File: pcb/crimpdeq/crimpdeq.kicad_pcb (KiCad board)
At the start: 4 copper layers, 30 x 30 mm, 51 parts, among them J2 USB4105-GF-A, J3 Loadcell_Pads, J4 Power_Sense_Pads, Q1 SS8550, Q2 DMG3415U, U1 ESP32-C3-MINI-1, U2 MCP73831T-2ACI/OT, U3 HX711, U5 MAX17048G+T10, U6 SY8088

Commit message: feat: split cable pads into independent battery and sense points
Replace the shared J4 multi-pad header with separate THT pads so B+/B-,
SW+/SW-, and A+/A- can be wired independently, and place the battery
column clear of USB/power copper.

Co-authored-by: Cursor <cursoragent@cursor.com>
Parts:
- removed J4: Power_Sense_Pads, External_Cable_Pads_Right
- added J10: A-_Cable_Pad, TestPoint:TestPoint_THTPad_D1.5mm_Drill0.7mm, F.Cu at (131.6, 81.1)
- added J5: B-_Cable_Pad, TestPoint:TestPoint_THTPad_D1.5mm_Drill0.7mm, F.Cu at (156.2, 73.5)
- added J6: SW+_Cable_Pad, TestPoint:TestPoint_THTPad_D1.5mm_Drill0.7mm, F.Cu at (156.2, 78.5)
- added J7: B+_Cable_Pad, TestPoint:TestPoint_THTPad_D1.5mm_Drill0.7mm, F.Cu at (156.2, 76.0)
- added J8: SW-_Cable_Pad, TestPoint:TestPoint_THTPad_D1.5mm_Drill0.7mm, F.Cu at (156.2, 81.1)
- added J9: A+_Cable_Pad, TestPoint:TestPoint_THTPad_D1.5mm_Drill0.7mm, F.Cu at (134.4, 81.1)
- R20, R21, R22: footprint R_0402_1005Metric -> Resistor_SMD:R_0402_1005Metric
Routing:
- net +BATT: track 43.7 -> 47.4 mm, vias 2 -> 3
- net SW_BATT: track 11.7 -> 13.8 mm
- net GND: track 215.7 -> 217.7 mm
- net VBUS: vias 2 -> 3
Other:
- board text added: "A+"
- board text added: "A-"
- board text added: "B+"
- board text added: "B-"
- board text added: "SW+"
- board text added: "SW-"

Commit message: fix: clean up cable-pad silk, Q2 symbol, and verification golden
Align the board with the post-split review: correct silk and shell vias,
use a pin-compatible PMOS symbol for DMG3415U, and update BOM/CPL/verify
for independent J5–J10 pads.

Co-authored-by: Cursor <cursoragent@cursor.com>
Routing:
- net Net-(J2-SHELL_GND-PadS1): track 33.6 -> 35.0 mm
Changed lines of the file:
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@@
 			(at 0 -1.648 0)
 			(layer "F.SilkS")
+			(hide yes)
 			(effects
 				(font
@@
 			(at 0 1.75 0)
 			(layer "F.Fab")
+			(hide yes)
 			(effects
 				(font
@@
 		(sheetname "/")
 		(sheetfile "crimpdeq.kicad_sch")
-		(units
-			(unit
-				(name "A")
-				(pins "1" "2")
-			)
-		)
 		(attr smd)
 		(duplicate_pad_numbers_are_jumpers no)
@@
 			(at 0 -1.648 0)
 			(layer "F.SilkS")
+			(hide yes)
 			(effects
 				(font
@@
 			(at 0 -1.648 0)
 			(layer "F.SilkS")
+			(hide yes)
 			(effects
 				(font
@@
 		(sheetname "/")
 		(sheetfile "crimpdeq.kicad_sch")
-		(units
-			(unit
-				(name "A")
-				(pins "1" "2")
-			)
-		)
 		(attr smd)
 		(duplicate_pad_numbers_are_jumpers no)
@@
 			(at 0 -1.648 0)
 			(layer "F.SilkS")
+			(hide yes)
 			(effects
 				(font
@@
 			(at 0 1.75 0)
 			(layer "F.Fab")
+			(hide yes)
 			(effects
 				(font
@@
 			(at 0 -1.648 0)
 			(layer "F.SilkS")
+			(hide yes)
 			(effects
 				(font
@@
 			(at 0 -1.648 0)
 			(layer "F.SilkS")
+			(hide yes)
 			(effects
 				(font
@@
 		(layer "Edge.Cuts")
 	)
-	(gr_text "SW+"
-		(at 154.5 66.7 0)
-		(layer "F.SilkS")
-		(effects
-			(font
-				(size 0.7 0.7)
-				(thickness 0.105)
-			)
-		)
-	)
-	(gr_text "SW-"
-		(at 154.5 69.3 0)
-		(layer "F.SilkS")
-		(effects
-			(font
-				(size 0.7 0.7)
-				(thickness 0.105)
-			)
-		)
-	)
-	(gr_text "B-"
-		(at 154.7 61.5 0)
-		(layer "F.SilkS")
-		(effects
-			(font
-				(size 0.7 0.7)
-				(thickness 0.105)
-			)
-		)
-	)
-	(gr_text "B+"
-		(at 154.7 64.099999 0)
-		(layer "F.SilkS")
-		(effects
-			(font
-				(size 0.7 0.7)
-				(thickness 0.105)
-			)
-		)
-	)
 	(gr_text "A-"
-		(at 131.6 79.7 0)
+		(at 131.6 79.5 0)
 		(layer "F.SilkS")
 		(effects
@@
 	)
 	(gr_text "A+"
-		(at 134.4 79.7 0)
+		(at 134.4 79.5 0)
 		(layer "F.SilkS")
 		(effects
@@
 		)
 	)
-	(gr_text "SW+"
-		(at 151.8 79.2 0)
+	(gr_text "B-"
+		(at 153.5 73.5 0)
 		(layer "F.SilkS")
 		(effects
@@
 		)
 	)
-	(gr_text "B+"
-		(at 152.3 76.2 0)
+	(gr_text "SW+"
+		(at 153.8 78.55 0)
 		(layer "F.SilkS")
 		(effects
@@
 	)
 	(gr_text "SW-"
-		(at 155.2 79.2 0)
+		(at 153.8 81.1 0)
 		(layer "F.SilkS")
 		(effects
@@
 		)
 	)
-	(gr_text "B-"
-		(at 155.5 75.7 0)
+	(gr_text "B+"
+		(at 154 76 0)
 		(layer "F.SilkS")
 		(effects
@@
 	)
 	(segment
+		(start 152 76)
+		(end 151.32 76)
+		(width 0.25)
+		(layer "B.Cu")
+		(net "Net-(J2-SHELL_GND-PadS1)")
+	)
+	(segment
 		(start 146.49 70.5)
 		(end 141 70.5)
@@
 		(layer "B.Cu")
 		(net "Net-(J2-SHELL_GND-PadS1)")
+	)
+	(segment
+		(start 142 76)
+		(end 142.68 76)
+		(width 0.25)
+		(layer "B.Cu")
+		(net "Net-(J2-SHELL_GND-PadS1)")

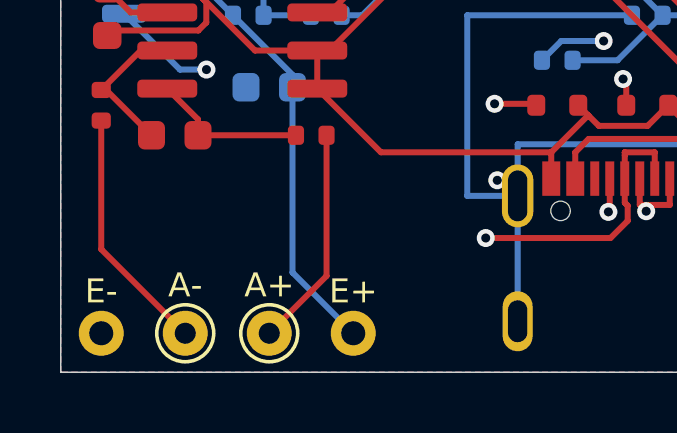
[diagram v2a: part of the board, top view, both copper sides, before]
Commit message: feat: replace J3/U4 with independent E+ and E- cable pads
Make excitation pads match the other single-pad connectors, drop the
board-only J3 footprint and U4 harness symbol, and refresh schematic
layout plus verification/assembly artifacts.

Co-authored-by: Cursor <cursoragent@cursor.com>
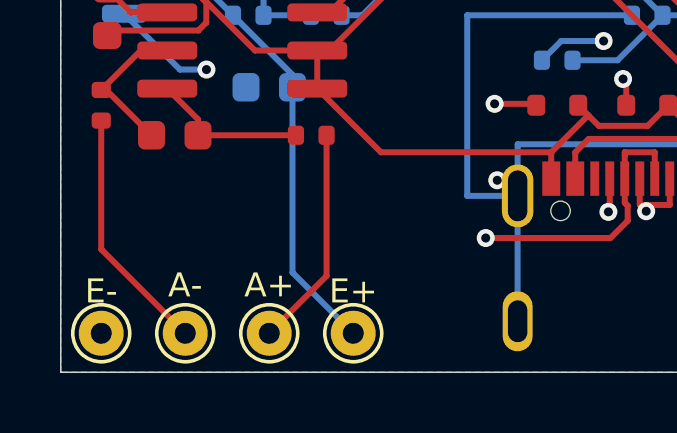
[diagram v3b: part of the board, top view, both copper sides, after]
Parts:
- removed J3: Loadcell_Pads, External_Cable_Pads_Left
- added J11: E+_Cable_Pad, TestPoint:TestPoint_THTPad_D1.5mm_Drill0.7mm, F.Cu at (137.2, 81.1)
- added J12: E-_Cable_Pad, TestPoint:TestPoint_THTPad_D1.5mm_Drill0.7mm, F.Cu at (128.8, 81.1)
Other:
- board text added: "E+"
- board text added: "E-"
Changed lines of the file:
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@@
 		)
 	)
-	(footprint "External_Cable_Pads_Left"
-		(layer "F.Cu")
-		(at 151.2 55.75)
-		(property "Reference" "J3"
-			(at 0 -4 0)
-			(layer "F.SilkS")
-			(hide yes)
-			(effects
-				(font
-					(size 1 1)
-					(thickness 0.15)
-				)
-			)
-		)
-		(property "Value" "Loadcell_Pads"
-			(at 0 4 0)
-			(layer "F.Fab")
-			(hide yes)
-			(effects
-				(font
-					(size 1 1)
-					(thickness 0.15)
-				)
-			)
-		)
-		(property "Datasheet" ""
-			(at 0 0 0)
-			(layer "F.Fab")
-			(hide yes)
-			(effects
-				(font
-					(size 1 1)
-					(thickness 0.15)
-				)
-			)
-		)
-		(property "Description" ""
-			(at 0 0 0)
-			(layer "F.Fab")
-			(hide yes)
-			(effects
-				(font
-					(size 1 1)
-					(thickness 0.15)
-				)
-			)
-		)
-		(attr through_hole board_only)
-		(duplicate_pad_numbers_are_jumpers no)
-		(fp_text user "E-"
-			(at -22.4 23.95 0)
-			(layer "F.SilkS")
-			(effects
-				(font
-					(size 0.8 0.8)
-					(thickness 0.15)
-				)
-			)
-		)
-		(fp_text user "E+"
-			(at -14 23.95 0)
-			(layer "F.SilkS")
-			(effects
-				(font
-					(size 0.8 0.8)
-					(thickness 0.15)
-				)
-			)
-		)
-		(pad "1" thru_hole circle
-			(at -14 25.35)
-			(size 1.5 1.5)
-			(drill 0.8)
-			(layers "*.Cu" "*.Mask")
-			(remove_unused_layers no)
-			(net "E+")
-			(pinfunction "E+")
-			(pintype "passive")
-		)
-		(pad "2" thru_hole circle
-			(at -22.4 25.35)
-			(size 1.5 1.5)
-			(drill 0.8)
-			(layers "*.Cu" "*.Mask")
-			(remove_unused_layers no)
-			(net "GND")
-			(pinfunction "E-")
-			(pintype "passive")
-		)
-		(embedded_fonts no)
-	)
 	(footprint "Resistor_SMD:R_0402_1005Metric"
 		(layer "F.Cu")
@@
 	(footprint "TestPoint:TestPoint_THTPad_D1.5mm_Drill0.7mm"
 		(layer "F.Cu")
+		(at 137.2 81.1)
+		(descr "THT pad as test Point, diameter 1.5mm, hole diameter 0.7mm")
+		(tags "test point THT pad")
+		(property "Reference" "J11"
+			(at 0 -1.648 0)
+			(layer "F.SilkS")
+			(hide yes)
+			(effects
+				(font
+					(size 1 1)
+					(thickness 0.15)
+				)
+			)
+		)
+		(property "Value" "E+_Cable_Pad"
+			(at 0 1.75 0)
+			(layer "F.Fab")
+			(hide yes)
+			(effects
+				(font
+					(size 1 1)
+					(thickness 0.15)
+				)
+			)
+		)
+		(property "Datasheet" ""
+			(at 0 0 0)
+			(unlocked yes)
+			(layer "F.Fab")
+			(hide yes)
+			(effects
+				(font
+					(size 1.27 1.27)
+					(thickness 0.15)
+				)
+			)
+		)
+		(property "Description" ""
+			(at 0 0 0)
+			(unlocked yes)
+			(layer "F.Fab")
+			(hide yes)
+			(effects
+				(font
+					(size 1.27 1.27)
+					(thickness 0.15)
+				)
+			)
+		)
+		(duplicate_pad_numbers_are_jumpers no)
+		(fp_circle
+			(center 0 0)
+			(end 0 0.95)
+			(stroke
+				(width 0.12)
+				(type solid)
+			)
+			(fill no)
+			(layer "F.SilkS")
+		)
+		(fp_circle
+			(center 0 0)
+			(end 1.25 0)
+			(stroke
+				(width 0.05)
+				(type solid)
+			)
+			(fill no)
+			(layer "F.CrtYd")
+		)
+		(fp_text user "${REFERENCE}"
+			(at 0 -1.65 0)
+			(layer "F.Fab")
+			(effects
+				(font
+					(size 1 1)
+					(thickness 0.15)
+				)
+			)
+		)
+		(pad "1" thru_hole circle
+			(at 0 0)
+			(size 1.5 1.5)
+			(drill 0.7)
+			(layers "*.Cu" "*.Mask")
+			(remove_unused_layers no)
+			(net "E+")
+		)
+		(embedded_fonts no)
+	)
+	(footprint "TestPoint:TestPoint_THTPad_D1.5mm_Drill0.7mm"
+		(layer "F.Cu")
 		(at 131.6 81.1)
 		(descr "THT pad as test Point, diameter 1.5mm, hole diameter 0.7mm")
@@
 		)
 	)
+	(footprint "TestPoint:TestPoint_THTPad_D1.5mm_Drill0.7mm"
+		(layer "F.Cu")
+		(at 128.8 81.1)
+		(descr "THT pad as test Point, diameter 1.5mm, hole diameter 0.7mm")
+		(tags "test point THT pad")
+		(property "Reference" "J12"
+			(at 0 -1.648 0)
+			(layer "F.SilkS")
+			(hide yes)
+			(effects
+				(font
+					(size 1 1)
+					(thickness 0.15)
+				)
+			)
+		)
+		(property "Value" "E-_Cable_Pad"
+			(at 0 1.75 0)
+			(layer "F.Fab")
+			(hide yes)
+			(effects
+				(font
+					(size 1 1)
+					(thickness 0.15)
+				)
+			)
+		)
+		(property "Datasheet" ""
+			(at 0 0 0)
+			(unlocked yes)
+			(layer "F.Fab")
+			(hide yes)
+			(effects
+				(font
+					(size 1.27 1.27)
+					(thickness 0.15)
+				)
+			)
+		)
+		(property "Description" ""
+			(at 0 0 0)
+			(unlocked yes)
+			(layer "F.Fab")
+			(hide yes)
+			(effects
+				(font
+					(size 1.27 1.27)
+					(thickness 0.15)
+				)
+			)
+		)
+		(duplicate_pad_numbers_are_jumpers no)
+		(fp_circle
+			(center 0 0)
+			(end 0 0.95)
+			(stroke
+				(width 0.12)
+				(type solid)
+			)
+			(fill no)
+			(layer "F.SilkS")
+		)
+		(fp_circle
+			(center 0 0)
+			(end 1.25 0)
+			(stroke
+				(width 0.05)
+				(type solid)
+			)
+			(fill no)
+			(layer "F.CrtYd")
+		)
+		(fp_text user "${REFERENCE}"
+			(at 0 -1.65 0)
+			(layer "F.Fab")
+			(effects
+				(font
+					(size 1 1)
+					(thickness 0.15)
+				)
+			)
+		)
+		(pad "1" thru_hole circle
+			(at 0 0)
+			(size 1.5 1.5)
+			(drill 0.7)
+			(layers "*.Cu" "*.Mask")
+			(remove_unused_layers no)
+			(net "GND")
+		)
+		(embedded_fonts no)
+	)
 	(footprint "Capacitor_SMD:C_0805_2012Metric"
 		(layer "F.Cu")
@@
 		)
 	)
+	(gr_text "E-"
+		(at 128.8 79.7 0)
+		(layer "F.SilkS")
+		(effects
+			(font
+				(size 0.8 0.8)
+				(thickness 0.15)
+			)
+		)
+	)
+	(gr_text "E+"
+		(at 137.2 79.7 0)
+		(layer "F.SilkS")
+		(effects
+			(font
+				(size 0.8 0.8)
+				(thickness 0.15)
+			)
+		)
+	)
 	(segment
 		(start 130.115 71.675)
@@
 	)
 	(segment
-		(start 130.4725 67.1225)
-		(end 131 66.595)
-		(width 0.2)
-		(layer "F.Cu")
-		(net "E+")
-	)
-	(segment
-		(start 129.5912 67.1225)
-		(end 130.4725 67.1225)
-		(width 0.2)
-		(layer "F.Cu")
-		(net "E+")
-	)
-	(via
-		(at 129.5912 67.1225)
-		(size 0.6)
-		(drill 0.3)
-		(layers "F.Cu" "B.Cu")
-		(net "E+")
-	)
-	(segment
-		(start 132.19 69.5)
-		(end 133.19 70.5)
-		(width 0.2)
-		(layer "B.Cu")
-		(net "E+")
-	)
-	(segment
-		(start 131.4375 69.5)
-		(end 132.19 69.5)
-		(width 0.2)
-		(layer "B.Cu")
-		(net "E+")
-	)
-	(segment
-		(start 135.175 72.485)
-		(end 135.175 72.9)
-		(width 0.2)
-		(layer "B.Cu")
-		(net "E+")
-	)
-	(segment
-		(start 135.175 72.9)
-		(end 135.175 79.075)
-		(width 0.2)
-		(layer "B.Cu")
-		(net "E+")
-	)
-	(segment
-		(start 133.19 70.5)
-		(end 135.175 72.485)
-		(width 0.2)
-		(layer "B.Cu")
-		(net "E+")
-	)
-	(segment
-		(start 135.175 79.075)
-		(end 137.2 81.1)
-		(width 0.2)
-		(layer "B.Cu")
-		(net "E+")
-	)
-	(segment
-		(start 137.2 81.1)
-		(end 129.5912 73.4912)
-		(width 0.2)
-		(layer "In2.Cu")
-		(net "E+")
-	)
-	(segment
-		(start 129.5912 73.4912)
-		(end 129.5912 67.1225)
-		(width 0.2)
-		(layer "In2.Cu")
-		(net "E+")
-	)
-	(segment
 		(start 149.8167 67.5895)
 		(end 150.852 67.5895)
@@
 	)
 	(segment
+		(start 130.4725 67.1225)
+		(end 131 66.595)
+		(width 0.2)
+		(layer "F.Cu")
+		(net "E+")
+	)
+	(segment
+		(start 129.5912 67.1225)
+		(end 130.4725 67.1225)
+		(width 0.2)
+		(layer "F.Cu")
+		(net "E+")
+	)
+	(via
+		(at 129.5912 67.1225)
+		(size 0.6)
+		(drill 0.3)
+		(layers "F.Cu" "B.Cu")
+		(net "E+")
+	)
+	(segment
+		(start 132.19 69.5)
+		(end 133.19 70.5)
+		(width 0.2)
+		(layer "B.Cu")
+		(net "E+")
+	)
+	(segment
+		(start 131.4375 69.5)
+		(end 132.19 69.5)
+		(width 0.2)
+		(layer "B.Cu")
+		(net "E+")
+	)
+	(segment
+		(start 135.175 72.485)
+		(end 135.175 72.9)
+		(width 0.2)
+		(layer "B.Cu")
+		(net "E+")
+	)
+	(segment
+		(start 135.175 72.9)
+		(end 135.175 79.075)
+		(width 0.2)
+		(layer "B.Cu")
+		(net "E+")
+	)
+	(segment
+		(start 133.19 70.5)
+		(end 135.175 72.485)
+		(width 0.2)
+		(layer "B.Cu")
+		(net "E+")
+	)
+	(segment
+		(start 135.175 79.075)
+		(end 137.2 81.1)
+		(width 0.2)
+		(layer "B.Cu")
+		(net "E+")
+	)
+	(segment
+		(start 137.2 81.1)
+		(end 129.5912 73.4912)
+		(width 0.2)
+		(layer "In2.Cu")
+		(net "E+")
+	)
+	(segment
+		(start 129.5912 73.4912)
+		(end 129.5912 67.1225)
+		(width 0.2)
+		(layer "In2.Cu")
+		(net "E+")
+	)
+	(segment

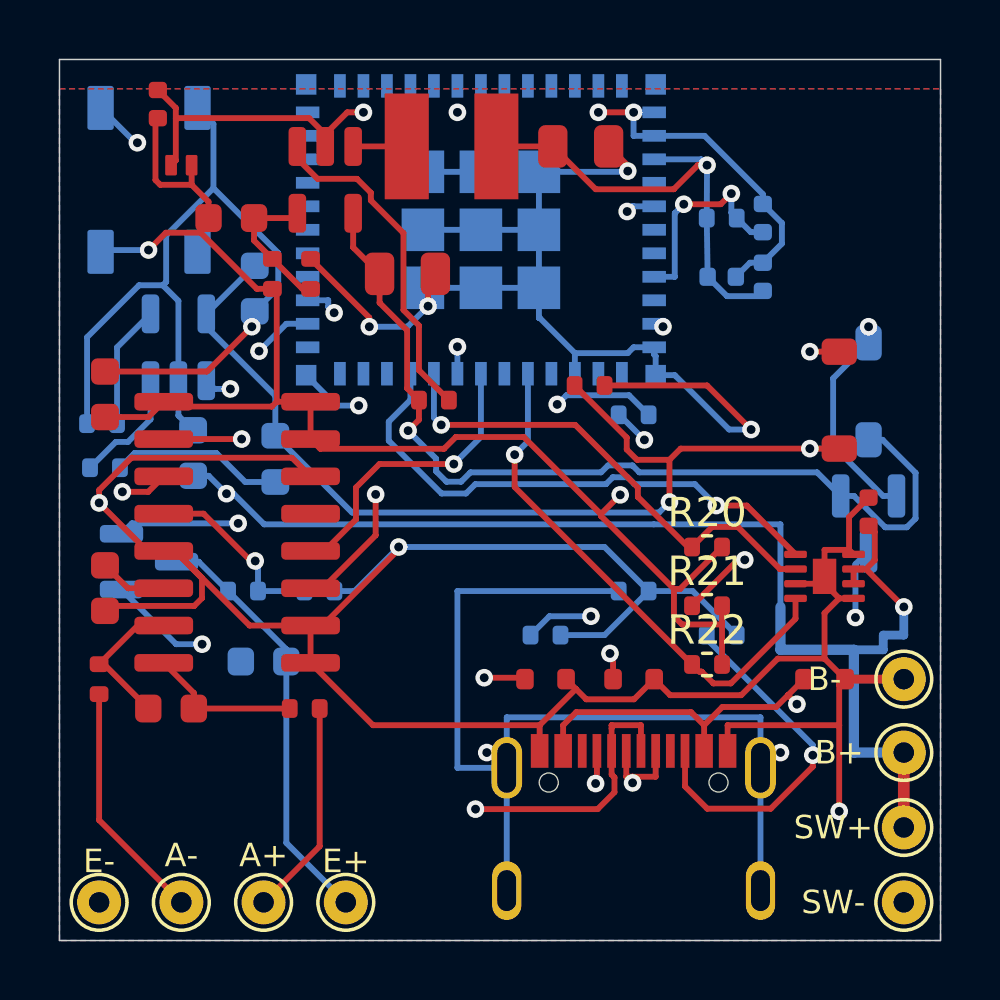
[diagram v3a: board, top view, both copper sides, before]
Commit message: feat: replace HX711 with ADS1220 ratiometric front-end
Swap U3 to ADS1220 TSSOP-16 with +3V3 excitation and 4-wire SPI, drop the
HX711 bias network, and document on-demand Freerouting instead of vendoring JREs.

Co-authored-by: Cursor <cursoragent@cursor.com>
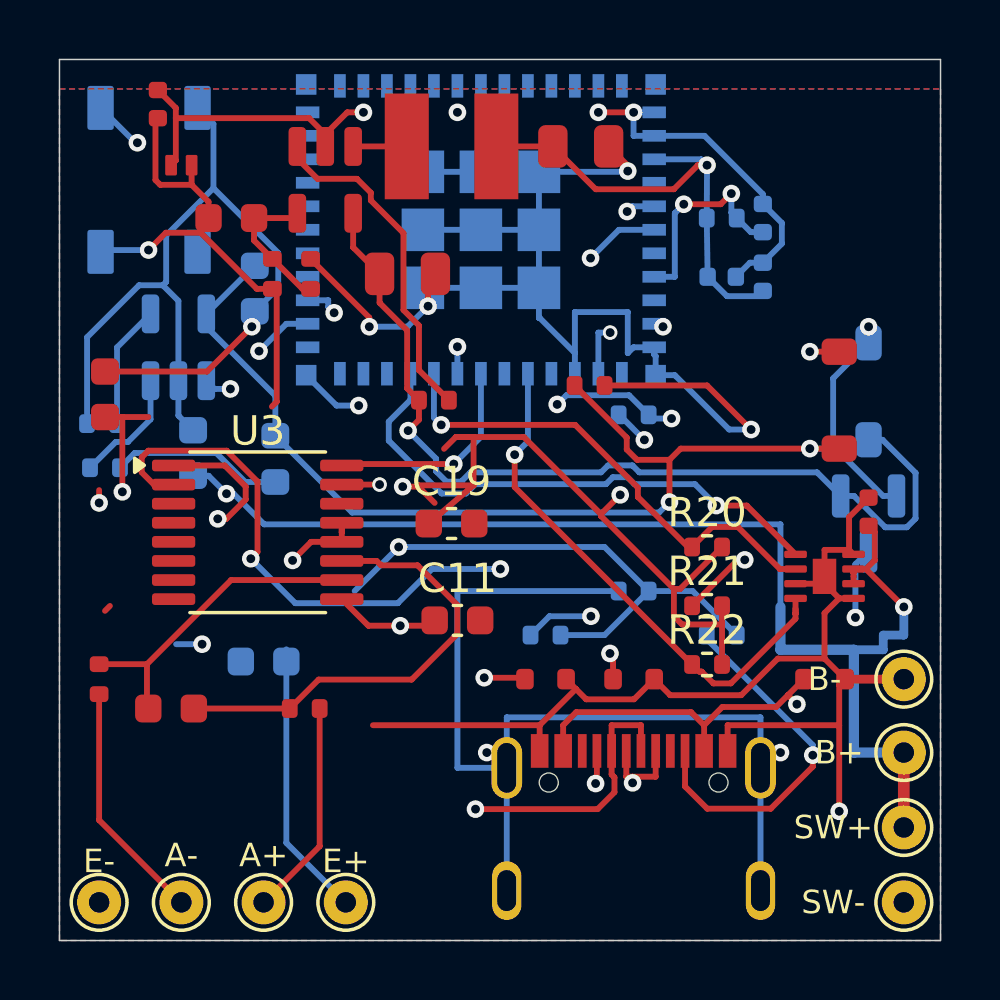
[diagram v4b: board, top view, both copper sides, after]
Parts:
- removed Q1: SS8550, Package_TO_SOT_SMD:SOT-23
- removed R5: 12kR 1%, Resistor_SMD:R_0402_1005Metric
- removed R6: 8k2R 1%, Resistor_SMD:R_0402_1005Metric
- added C19: 0.1uF, C_0603_1608Metric, F.Cu at (140.8, 68.2)
- C11: footprint Capacitor_SMD:C_0603_1608Metric -> C_0603_1608Metric
- U3: value HX711 -> ADS1220; footprint Package_SO:SOP-16_3.9x9.9mm_P1.27mm -> TSSOP-16_4.4x5mm_P0.65mm
- moved C11 12.1 mm to (141.0, 71.5), turned to 0 degrees
- moved U3 0.70 mm to (134.2, 68.5)
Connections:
- net /Buck_Coil renamed Buck_Coil
- C10 pad 1: E+ -> +3V3
- C11 pad 1: GND -> +3V3
- C11 pad 2: Net-(U3-VBG) -> GND
- C12 pad 1: Net-(U3-INA+) -> Net-(U3-AIN0)
- C12 pad 2: Net-(U3-INA-) -> Net-(U3-AIN1)
- J11 pad 1: E+ -> +3V3
- R7 pad 1: Net-(U3-INA+) -> Net-(U3-AIN0)
- R8 pad 1: Net-(U3-INA-) -> Net-(U3-AIN1)
- U1 pad 13: unconnected-(U1-GPIO1/ADC1_CH1/XTAL_32K_N-Pad13) -> IO1_MISO
- U1 pad 18: IO4_DATA -> IO4_MOSI
- U1 pad 6: unconnected-(U1-GPIO3/ADC1_CH3-Pad6) -> IO3_CS
- U3 pad 1: +3V3 -> IO5_SCK
- U3 pad 10: GND -> Net-(U3-AIN1)
- U3 pad 11: IO5_SCK -> Net-(U3-AIN0)
- U3 pad 12: IO4_DATA -> +3V3
- U3 pad 13: unconnected-(U3-XO-Pad13) -> +3V3
- U3 pad 14: GND -> unconnected-(U3-~{DRDY}-Pad14)
- U3 pad 15: +3V3 -> IO1_MISO
- U3 pad 16: +3V3 -> IO4_MOSI
- U3 pad 2: Net-(Q1-B) -> IO3_CS
- U3 pad 3: E+ -> GND
- U3 pad 4: Net-(U3-VFB) -> GND
- U3 pad 6: Net-(U3-VBG) -> unconnected-(U3-AIN3/REFN1-Pad6)
- U3 pad 7: Net-(U3-INA-) -> unconnected-(U3-AIN2-Pad7)
- U3 pad 8: Net-(U3-INA+) -> GND
- U3 pad 9: GND -> +3V3
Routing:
- net E+: track 33.2 -> 0.00 mm, vias 1 -> 0
- net IO3_CS: track 0.00 -> 33.0 mm, vias 0 -> 3
- net +3V3: track 94.4 -> 123.8 mm, vias 4 -> 8
- net GND: track 217.7 -> 189.0 mm
- net IO1_MISO: track 0.00 -> 24.3 mm, vias 0 -> 2
- net Net-(U3-AIN0): track 0.00 -> 15.6 mm
- net IO5_SCK: track 11.5 -> 25.5 mm
- net Net-(U3-AIN1): track 0.00 -> 11.0 mm
- net IO4_DATA: track 10.2 -> 0.00 mm, vias 1 -> 0
- net Net-(Q1-B): track 9.76 -> 0.00 mm, vias 2 -> 0
- net Net-(D4-DIN): track 23.2 -> 32.2 mm, vias 2 -> 3
- net IO4_MOSI: track 0.00 -> 7.33 mm, vias 0 -> 1
- net Net-(U3-VFB): track 6.43 -> 0.00 mm, vias 1 -> 0
- net Net-(U3-INA+): track 5.24 -> 0.00 mm
- net Net-(U3-INA-): track 5.05 -> 0.00 mm
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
